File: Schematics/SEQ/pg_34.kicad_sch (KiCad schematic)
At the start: 14 parts, among them U3501 F158, U3502 F158, U3503 F158, U3504 F158, U3505 F158, U3506 F158, U3507 F04, U3508 F240, U3509 F240, U3510 F04, U3511 F258, U3512 F258, U3513 F258, U3514 F258

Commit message: Much work on SEQ
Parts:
- removed U3504, U3505, U3506: F158, symbol r1000:F158
- removed U3508, U3509: F240, symbol r1000:F240
- removed U3510: F04, symbol r1000:F04
- removed U3511, U3512, U3513, U3514: F258, symbol r1000:F258
- U3501: value F158 -> XMUX24; symbol r1000:F158 -> r1000:XMUX24; Location F40 -> x99; Name CODMX0 -> CODMXS
- U3502: value F158 -> XBUF16; symbol r1000:F158 -> r1000:XBUF16; Location F39 -> x99; Name CODMX1 -> CODDR
- U3503: value F158 -> XMUX16; symbol r1000:F158 -> r1000:XMUX16; Location F36 -> x99; Name CODMX2 -> CODMXO
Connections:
- net BRANCH.IND~57: now also U3502.29 (I13)
- net BRANCH.IND~58: now also U3502.31 (I14)
- net BRANCH.IND~59: now also U3502.33 (I15)
- net BRANCH.OFFS~45: now also U3502.5 (I1)
- net BRANCH.OFFS~46: now also U3502.7 (I2)
- net BRANCH.OFFS~47: now also U3502.9 (I3)
- net BRANCH.OFFS~48: now also U3502.11 (I4)
- net BRANCH.OFFS~49: now also U3502.13 (I5)
- net BRANCH.OFFS~50: now also U3502.15 (I6)
- net BRANCH.OFFS~51: now also U3502.17 (I7)
- net BRANCH.OFFS~52: now also U3502.19 (I8)
- net BRANCH.OFFS~53: now also U3502.21 (I9)
- net BRANCH.OFFS~54: now also U3502.23 (I10)
- net BRANCH.OFFS~55: now also U3502.25 (I11)
- net BRANCH.OFFS~56: now also U3502.27 (I12)
- net CODE.IND57: now also U3502.30 (Y13), U3503.48 (Y13)
- net CODE.IND58: now also U3502.32 (Y14), U3503.50 (Y14)
- net CODE.IND59: now also U3502.34 (Y15), U3503.52 (Y15)
- net CODE.OFFS45: now also U3502.6 (Y1), U3503.24 (Y1)
- net CODE.OFFS46: now also U3502.8 (Y2), U3503.26 (Y2)
- net CODE.OFFS47: now also U3502.10 (Y3), U3503.28 (Y3)
- net CODE.OFFS48: now also U3502.12 (Y4), U3503.30 (Y4)
- net CODE.OFFS49: now also U3502.14 (Y5), U3503.32 (Y5)
- net CODE.OFFS50: now also U3502.16 (Y6), U3503.34 (Y6)
- net CODE.OFFS51: now also U3502.18 (Y7), U3503.36 (Y7)
- net CODE.OFFS52: now also U3502.20 (Y8), U3503.38 (Y8)
- net CODE.OFFS53: now also U3502.22 (Y9), U3503.40 (Y9)
- net CODE.OFFS54: now also U3502.24 (Y10), U3503.42 (Y10)
- net CODE.OFFS55: now also U3502.26 (Y11), U3503.44 (Y11)
- net CODE.OFFS56: now also U3502.28 (Y12), U3503.46 (Y12)
- net CODE.SEGN10: now also U3501.34 (Y2); no longer U3501.9 (Y2)
- net CODE.SEGN11: now also U3501.36 (Y3); no longer U3501.12 (Y3)
- net CODE.SEGN12: now also U3501.38 (Y4); no longer U3502.4 (Y0)
- net CODE.SEGN13: now also U3501.40 (Y5); no longer U3502.7 (Y1)
- net CODE.SEGN14: now also U3501.42 (Y6); no longer U3502.9 (Y2)
- net CODE.SEGN15: now also U3501.44 (Y7); no longer U3502.12 (Y3)
- net CODE.SEGN16: now also U3501.46 (Y8); no longer U3503.4 (Y0)
- net CODE.SEGN17: now also U3501.48 (Y9); no longer U3503.7 (Y1)
- net CODE.SEGN18: now also U3501.50 (Y10); no longer U3503.9 (Y2)
- net CODE.SEGN19: now also U3501.52 (Y11); no longer U3503.12 (Y3)
- net CODE.SEGN20: now also U3501.54 (Y12)
- net CODE.SEGN21: now also U3501.56 (Y13)
- net CODE.SEGN22: now also U3501.58 (Y14)
- net CODE.SEGN23: now also U3501.60 (Y15)
- net CODE.SEGN24: now also U3501.62 (Y16)
- net CODE.SEGN25: now also U3501.64 (Y17)
- net CODE.SEGN26: now also U3501.66 (Y18)
- net CODE.SEGN27: now also U3501.68 (Y19)
- net CODE.SEGN28: now also U3501.70 (Y20)
- net CODE.SEGN29: now also U3501.72 (Y21)
- net CODE.SEGN30: now also U3501.74 (Y22)
- net CODE.SEGN31: now also U3501.76 (Y23)
- net CODE.SEGN8: now also U3501.30 (Y0); no longer U3501.4 (Y0)
- net CODE.SEGN9: now also U3501.32 (Y1); no longer U3501.7 (Y1)
- net CODE_SEL.RND0: now also U3501.4 (S), U3503.4 (S); no longer U3501.1 (S), U3502.1 (S), U3503.1 (S)
- net CODE_SEL.RND1: now also U3503.8 (OE)
- net MACRO_PC.IND~57: now also U3503.47 (B13)
- net MACRO_PC.IND~58: now also U3503.49 (B14)
- net MACRO_PC.IND~59: now also U3503.51 (B15)
- net MACRO_PC.OFS~45: now also U3503.23 (B1)
- net MACRO_PC.OFS~46: now also U3503.25 (B2)
- net MACRO_PC.OFS~47: now also U3503.27 (B3)
- net MACRO_PC.OFS~48: now also U3503.29 (B4)
- net MACRO_PC.OFS~49: now also U3503.31 (B5)
- net MACRO_PC.OFS~50: now also U3503.33 (B6)
- net MACRO_PC.OFS~51: now also U3503.35 (B7)
- net MACRO_PC.OFS~52: now also U3503.37 (B8)
- net MACRO_PC.OFS~53: now also U3503.39 (B9)
- net MACRO_PC.OFS~54: now also U3503.41 (B10)
- net MACRO_PC.OFS~55: now also U3503.43 (B11)
- net MACRO_PC.OFS~56: now also U3503.45 (B12)
- net MACRO_PC.SEG~10: now also U3501.33 (B2); no longer U3501.10 (B2)
- net MACRO_PC.SEG~11: now also U3501.35 (B3); no longer U3501.13 (B3)
- net MACRO_PC.SEG~12: now also U3501.37 (B4); no longer U3502.3 (B0)
- net MACRO_PC.SEG~13: now also U3501.39 (B5); no longer U3502.6 (B1)
- net MACRO_PC.SEG~14: now also U3501.41 (B6); no longer U3502.10 (B2)
- net MACRO_PC.SEG~15: now also U3501.43 (B7); no longer U3502.13 (B3)
- net MACRO_PC.SEG~16: now also U3501.45 (B8); no longer U3503.3 (B0)
- net MACRO_PC.SEG~17: now also U3501.47 (B9); no longer U3503.6 (B1)
- net MACRO_PC.SEG~18: now also U3501.49 (B10); no longer U3503.10 (B2)
- net MACRO_PC.SEG~19: now also U3501.51 (B11); no longer U3503.13 (B3)
- net MACRO_PC.SEG~20: now also U3501.53 (B12)
- net MACRO_PC.SEG~21: now also U3501.55 (B13)
- net MACRO_PC.SEG~22: now also U3501.57 (B14)
- net MACRO_PC.SEG~23: now also U3501.59 (B15)
- net MACRO_PC.SEG~24: now also U3501.61 (B16)
- net MACRO_PC.SEG~25: now also U3501.63 (B17)
- net MACRO_PC.SEG~26: now also U3501.65 (B18)
- net MACRO_PC.SEG~27: now also U3501.67 (B19)
- net MACRO_PC.SEG~28: now also U3501.69 (B20)
- net MACRO_PC.SEG~29: now also U3501.71 (B21)
- net MACRO_PC.SEG~30: now also U3501.73 (B22)
- net MACRO_PC.SEG~31: now also U3501.75 (B23)
- net MACRO_PC.SEG~8: now also U3501.29 (B0); no longer U3501.3 (B0)
- net MACRO_PC.SEG~9: now also U3501.31 (B1); no longer U3501.6 (B1)
- net PD: now also U3501.2 (INV), U3501.6 (E), U3501.8 (OE), U3502.1 (INV), U3503.2 (INV), U3503.6 (E); no longer U3501.15 (E), U3502.15 (E), U3503.15 (E)
- net RETRN_PC.IND~57: now also U3503.18 (A13)
- net RETRN_PC.IND~58: now also U3503.19 (A14)
- net RETRN_PC.IND~59: now also U3503.20 (A15)
- net RETRN_PC.OFS~45: now also U3503.3 (A1)
- net RETRN_PC.OFS~46: now also U3503.5 (A2)
- net RETRN_PC.OFS~47: now also U3503.7 (A3)
- net RETRN_PC.OFS~48: now also U3503.9 (A4)
- net RETRN_PC.OFS~49: now also U3503.10 (A5)
- net RETRN_PC.OFS~50: now also U3503.11 (A6)
- net RETRN_PC.OFS~51: now also U3503.12 (A7)
- net RETRN_PC.OFS~52: now also U3503.13 (A8)
- net RETRN_PC.OFS~53: now also U3503.14 (A9)
- net RETRN_PC.OFS~54: now also U3503.15 (A10)
- net RETRN_PC.OFS~55: now also U3503.16 (A11)
- net RETRN_PC.OFS~56: now also U3503.17 (A12)
- net RETRN_PC.SEG~10: now also U3501.5 (A2); no longer U3501.11 (A2)
- net RETRN_PC.SEG~11: now also U3501.7 (A3); no longer U3501.14 (A3)
- net RETRN_PC.SEG~12: now also U3501.9 (A4); no longer U3502.2 (A0)
- net RETRN_PC.SEG~13: now also U3501.10 (A5); no longer U3502.5 (A1)
- net RETRN_PC.SEG~14: now also U3501.11 (A6); no longer U3502.11 (A2)
- net RETRN_PC.SEG~15: now also U3501.12 (A7); no longer U3502.14 (A3)
- net RETRN_PC.SEG~16: now also U3501.13 (A8); no longer U3503.2 (A0)
- net RETRN_PC.SEG~17: now also U3501.14 (A9); no longer U3503.5 (A1)
- net RETRN_PC.SEG~18: now also U3501.15 (A10); no longer U3503.11 (A2)
- net RETRN_PC.SEG~19: now also U3501.16 (A11); no longer U3503.14 (A3)
- net RETRN_PC.SEG~20: now also U3501.17 (A12)
- net RETRN_PC.SEG~21: now also U3501.18 (A13)
- net RETRN_PC.SEG~22: now also U3501.19 (A14)
- net RETRN_PC.SEG~23: now also U3501.20 (A15)
- net RETRN_PC.SEG~24: now also U3501.21 (A16)
- net RETRN_PC.SEG~25: now also U3501.22 (A17)
- net RETRN_PC.SEG~26: now also U3501.23 (A18)
- net RETRN_PC.SEG~27: now also U3501.24 (A19)
- net RETRN_PC.SEG~28: now also U3501.25 (A20)
- net RETRN_PC.SEG~29: now also U3501.26 (A21)
- net RETRN_PC.SEG~30: now also U3501.27 (A22)
- net RETRN_PC.SEG~31: now also U3501.28 (A23)
- net RETRN_PC.SEG~8: now also U3501.1 (A0); no longer U3501.2 (A0)
- net RETRN_PC.SEG~9: now also U3501.3 (A1); no longer U3501.5 (A1)
- net at U3507.2 (Q): now also U3502.2 (OE)
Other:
- moved on the sheet: U3507

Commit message: KiCad 6
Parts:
- U3501: value XMUX24 -> (none)
- U3502: value XBUF16 -> (none)
- U3503: value XMUX16 -> (none)
- U3507: value F04 -> (none)

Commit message: Recover from KiCad-6 munging
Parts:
- U3501: value (none) -> XMUX24
- U3502: value (none) -> XBUF16
- U3503: value (none) -> XMUX16
- U3507: value (none) -> F04

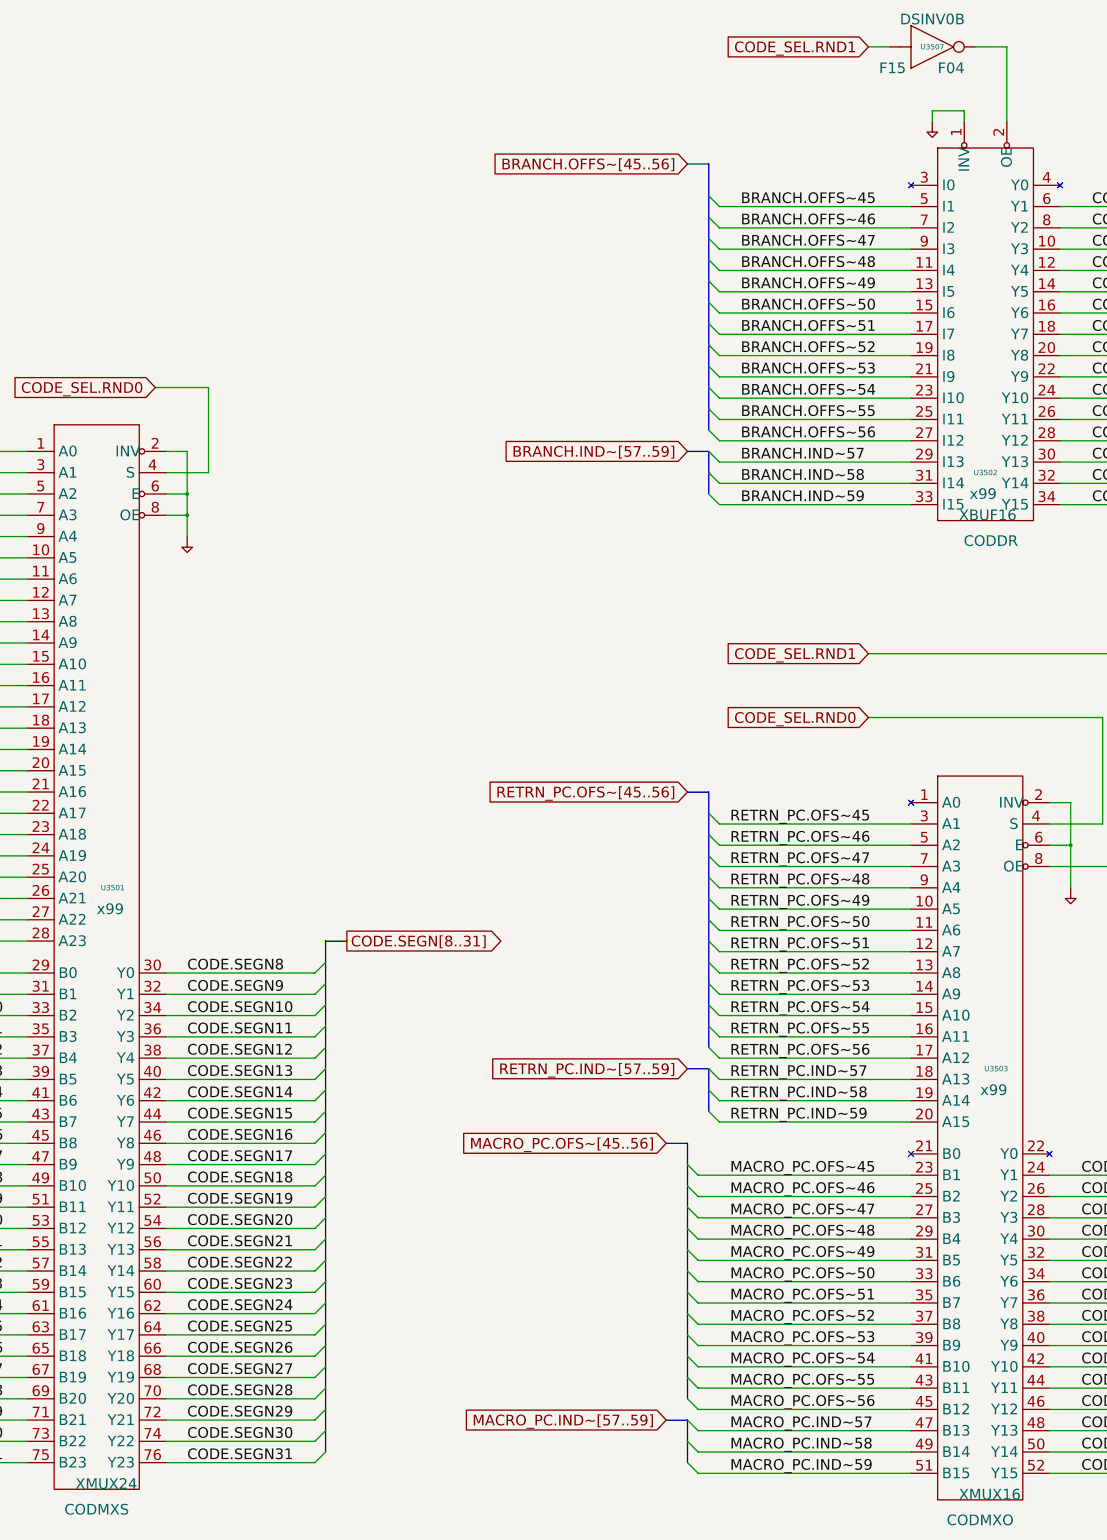
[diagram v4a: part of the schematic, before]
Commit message: Fix polarity of unused part of driven FIU bus.
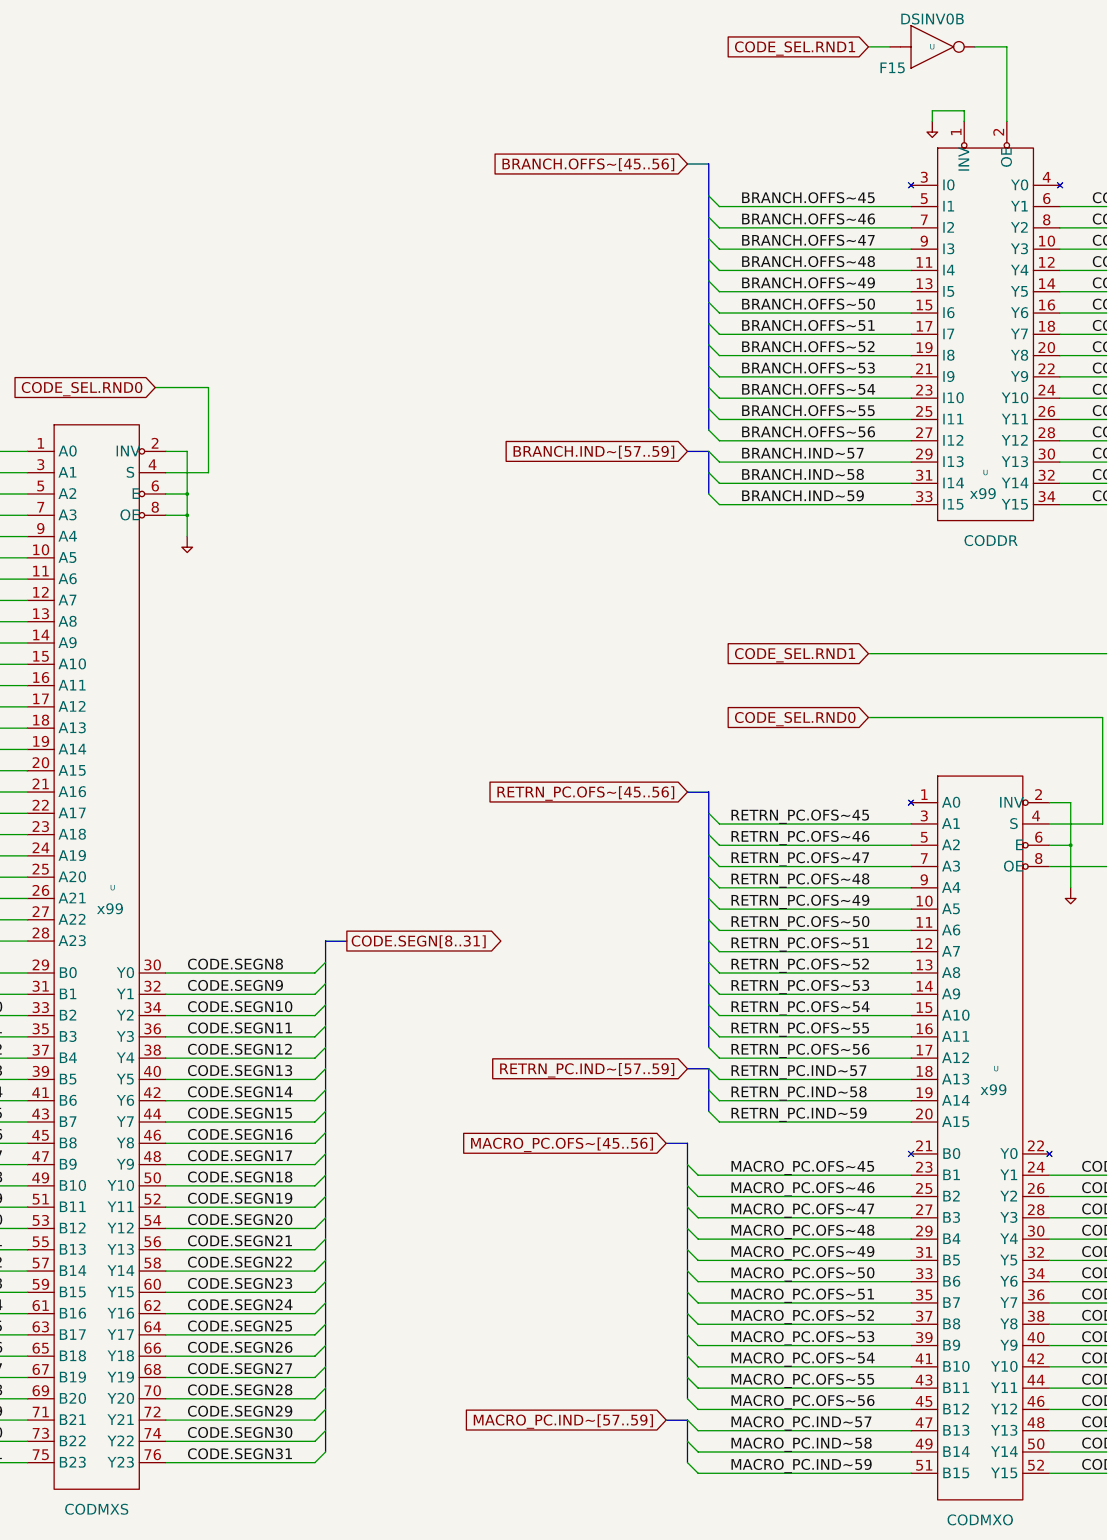
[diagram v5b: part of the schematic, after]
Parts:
- removed U3501: XMUX24, symbol r1000:XMUX24
- removed U3502: XBUF16, symbol r1000:XBUF16
- removed U3503: XMUX16, symbol r1000:XMUX16
- removed U3507: F04, symbol r1000:F04
- added U: (no value), symbol r1000:F04
- added U: (no value), symbol r1000:XBUF16
- added U: (no value), symbol r1000:XMUX24
- added U: (no value), symbol r1000:XMUX16
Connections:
- net BRANCH.IND~57: now also U.29 (I13)
- net BRANCH.IND~58: now also U.31 (I14)
- net BRANCH.IND~59: now also U.33 (I15)
- net BRANCH.OFFS~45: now also U.5 (I1)
- net BRANCH.OFFS~46: now also U.7 (I2)
- net BRANCH.OFFS~47: now also U.9 (I3)
- net BRANCH.OFFS~48: now also U.11 (I4)
- net BRANCH.OFFS~49: now also U.13 (I5)
- net BRANCH.OFFS~50: now also U.15 (I6)
- net BRANCH.OFFS~51: now also U.17 (I7)
- net BRANCH.OFFS~52: now also U.19 (I8)
- net BRANCH.OFFS~53: now also U.21 (I9)
- net BRANCH.OFFS~54: now also U.23 (I10)
- net BRANCH.OFFS~55: now also U.25 (I11)
- net BRANCH.OFFS~56: now also U.27 (I12)
- net CODE.IND57: now also U.30 (Y13), U.48 (Y13)
- net CODE.IND58: now also U.32 (Y14), U.50 (Y14)
- net CODE.IND59: now also U.34 (Y15), U.52 (Y15)
- net CODE.OFFS45: now also U.24 (Y1), U.6 (Y1)
- net CODE.OFFS46: now also U.26 (Y2), U.8 (Y2)
- net CODE.OFFS47: now also U.10 (Y3), U.28 (Y3)
- net CODE.OFFS48: now also U.12 (Y4), U.30 (Y4)
- net CODE.OFFS49: now also U.14 (Y5), U.32 (Y5)
- net CODE.OFFS50: now also U.16 (Y6), U.34 (Y6)
- net CODE.OFFS51: now also U.18 (Y7), U.36 (Y7)
- net CODE.OFFS52: now also U.20 (Y8), U.38 (Y8)
- net CODE.OFFS53: now also U.22 (Y9), U.40 (Y9)
- net CODE.OFFS54: now also U.24 (Y10), U.42 (Y10)
- net CODE.OFFS55: now also U.26 (Y11), U.44 (Y11)
- net CODE.OFFS56: now also U.28 (Y12), U.46 (Y12)
- net CODE.SEGN10: now also U.34 (Y2)
- net CODE.SEGN11: now also U.36 (Y3)
- net CODE.SEGN12: now also U.38 (Y4)
- net CODE.SEGN13: now also U.40 (Y5)
- net CODE.SEGN14: now also U.42 (Y6)
- net CODE.SEGN15: now also U.44 (Y7)
- net CODE.SEGN16: now also U.46 (Y8)
- net CODE.SEGN17: now also U.48 (Y9)
- net CODE.SEGN18: now also U.50 (Y10)
- net CODE.SEGN19: now also U.52 (Y11)
- net CODE.SEGN20: now also U.54 (Y12)
- net CODE.SEGN21: now also U.56 (Y13)
- net CODE.SEGN22: now also U.58 (Y14)
- net CODE.SEGN23: now also U.60 (Y15)
- net CODE.SEGN24: now also U.62 (Y16)
- net CODE.SEGN25: now also U.64 (Y17)
- net CODE.SEGN26: now also U.66 (Y18)
- net CODE.SEGN27: now also U.68 (Y19)
- net CODE.SEGN28: now also U.70 (Y20)
- net CODE.SEGN29: now also U.72 (Y21)
- net CODE.SEGN30: now also U.74 (Y22)
- net CODE.SEGN31: now also U.76 (Y23)
- net CODE.SEGN8: now also U.30 (Y0)
- net CODE.SEGN9: now also U.32 (Y1)
- net CODE_SEL.RND0: now also U.4 (S), U.4 (S)
- net CODE_SEL.RND1: now also U.1 (D0), U.8 (OE)
- net MACRO_PC.IND~57: now also U.47 (B13)
- net MACRO_PC.IND~58: now also U.49 (B14)
- net MACRO_PC.IND~59: now also U.51 (B15)
- net MACRO_PC.OFS~45: now also U.23 (B1)
- net MACRO_PC.OFS~46: now also U.25 (B2)
- net MACRO_PC.OFS~47: now also U.27 (B3)
- net MACRO_PC.OFS~48: now also U.29 (B4)
- net MACRO_PC.OFS~49: now also U.31 (B5)
- net MACRO_PC.OFS~50: now also U.33 (B6)
- net MACRO_PC.OFS~51: now also U.35 (B7)
- net MACRO_PC.OFS~52: now also U.37 (B8)
- net MACRO_PC.OFS~53: now also U.39 (B9)
- net MACRO_PC.OFS~54: now also U.41 (B10)
- net MACRO_PC.OFS~55: now also U.43 (B11)
- net MACRO_PC.OFS~56: now also U.45 (B12)
- net MACRO_PC.SEG~10: now also U.33 (B2)
- net MACRO_PC.SEG~11: now also U.35 (B3)
- net MACRO_PC.SEG~12: now also U.37 (B4)
- net MACRO_PC.SEG~13: now also U.39 (B5)
- net MACRO_PC.SEG~14: now also U.41 (B6)
- net MACRO_PC.SEG~15: now also U.43 (B7)
- net MACRO_PC.SEG~16: now also U.45 (B8)
- net MACRO_PC.SEG~17: now also U.47 (B9)
- net MACRO_PC.SEG~18: now also U.49 (B10)
- net MACRO_PC.SEG~19: now also U.51 (B11)
- net MACRO_PC.SEG~20: now also U.53 (B12)
- net MACRO_PC.SEG~21: now also U.55 (B13)
- net MACRO_PC.SEG~22: now also U.57 (B14)
- net MACRO_PC.SEG~23: now also U.59 (B15)
- net MACRO_PC.SEG~24: now also U.61 (B16)
- net MACRO_PC.SEG~25: now also U.63 (B17)
- net MACRO_PC.SEG~26: now also U.65 (B18)
- net MACRO_PC.SEG~27: now also U.67 (B19)
- net MACRO_PC.SEG~28: now also U.69 (B20)
- net MACRO_PC.SEG~29: now also U.71 (B21)
- net MACRO_PC.SEG~30: now also U.73 (B22)
- net MACRO_PC.SEG~31: now also U.75 (B23)
- net MACRO_PC.SEG~8: now also U.29 (B0)
- net MACRO_PC.SEG~9: now also U.31 (B1)
- net PD: now also U.1 (INV), U.2 (INV), U.2 (INV), U.6 (E), U.6 (E), U.8 (OE)
- net RETRN_PC.IND~57: now also U.18 (A13)
- net RETRN_PC.IND~58: now also U.19 (A14)
- net RETRN_PC.IND~59: now also U.20 (A15)
- net RETRN_PC.OFS~45: now also U.3 (A1)
- net RETRN_PC.OFS~46: now also U.5 (A2)
- net RETRN_PC.OFS~47: now also U.7 (A3)
- net RETRN_PC.OFS~48: now also U.9 (A4)
- net RETRN_PC.OFS~49: now also U.10 (A5)
- net RETRN_PC.OFS~50: now also U.11 (A6)
- net RETRN_PC.OFS~51: now also U.12 (A7)
- net RETRN_PC.OFS~52: now also U.13 (A8)
- net RETRN_PC.OFS~53: now also U.14 (A9)
- net RETRN_PC.OFS~54: now also U.15 (A10)
- net RETRN_PC.OFS~55: now also U.16 (A11)
- net RETRN_PC.OFS~56: now also U.17 (A12)
- net RETRN_PC.SEG~10: now also U.5 (A2)
- net RETRN_PC.SEG~11: now also U.7 (A3)
- net RETRN_PC.SEG~12: now also U.9 (A4)
- net RETRN_PC.SEG~13: now also U.10 (A5)
- net RETRN_PC.SEG~14: now also U.11 (A6)
- net RETRN_PC.SEG~15: now also U.12 (A7)
- net RETRN_PC.SEG~16: now also U.13 (A8)
- net RETRN_PC.SEG~17: now also U.14 (A9)
- net RETRN_PC.SEG~18: now also U.15 (A10)
- net RETRN_PC.SEG~19: now also U.16 (A11)
- net RETRN_PC.SEG~20: now also U.17 (A12)
- net RETRN_PC.SEG~21: now also U.18 (A13)
- net RETRN_PC.SEG~22: now also U.19 (A14)
- net RETRN_PC.SEG~23: now also U.20 (A15)
- net RETRN_PC.SEG~24: now also U.21 (A16)
- net RETRN_PC.SEG~25: now also U.22 (A17)
- net RETRN_PC.SEG~26: now also U.23 (A18)
- net RETRN_PC.SEG~27: now also U.24 (A19)
- net RETRN_PC.SEG~28: now also U.25 (A20)
- net RETRN_PC.SEG~29: now also U.26 (A21)
- net RETRN_PC.SEG~30: now also U.27 (A22)
- net RETRN_PC.SEG~31: now also U.28 (A23)
- net RETRN_PC.SEG~8: now also U.1 (A0)
- net RETRN_PC.SEG~9: now also U.3 (A1)
- new net: U.2 (OE), U.2 (Q)
